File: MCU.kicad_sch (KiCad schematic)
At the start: 14 parts, among them Q15 LMBT3904DW1T1G, SW3 SKRKAEE020, U1 ESP32-S3-WROOM-1U-N16, U15 TPS3831G33DQNR, U3 CH343P

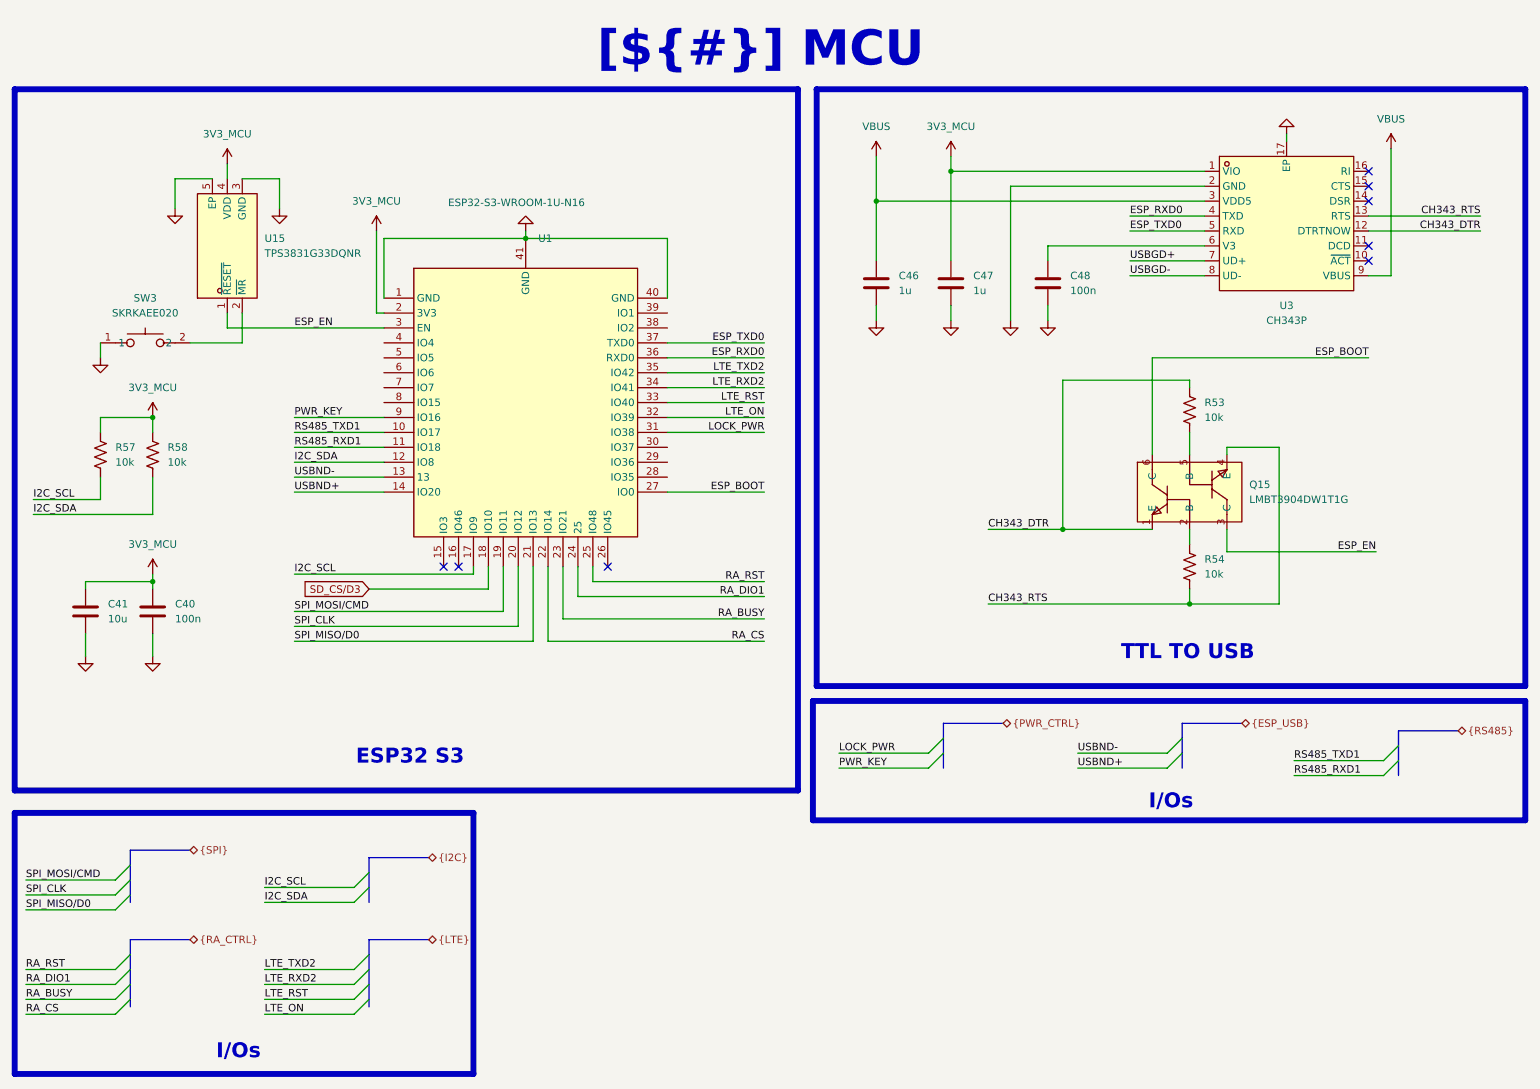
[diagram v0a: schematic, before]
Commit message: [Schematic][Added] Project Architecture, connectors
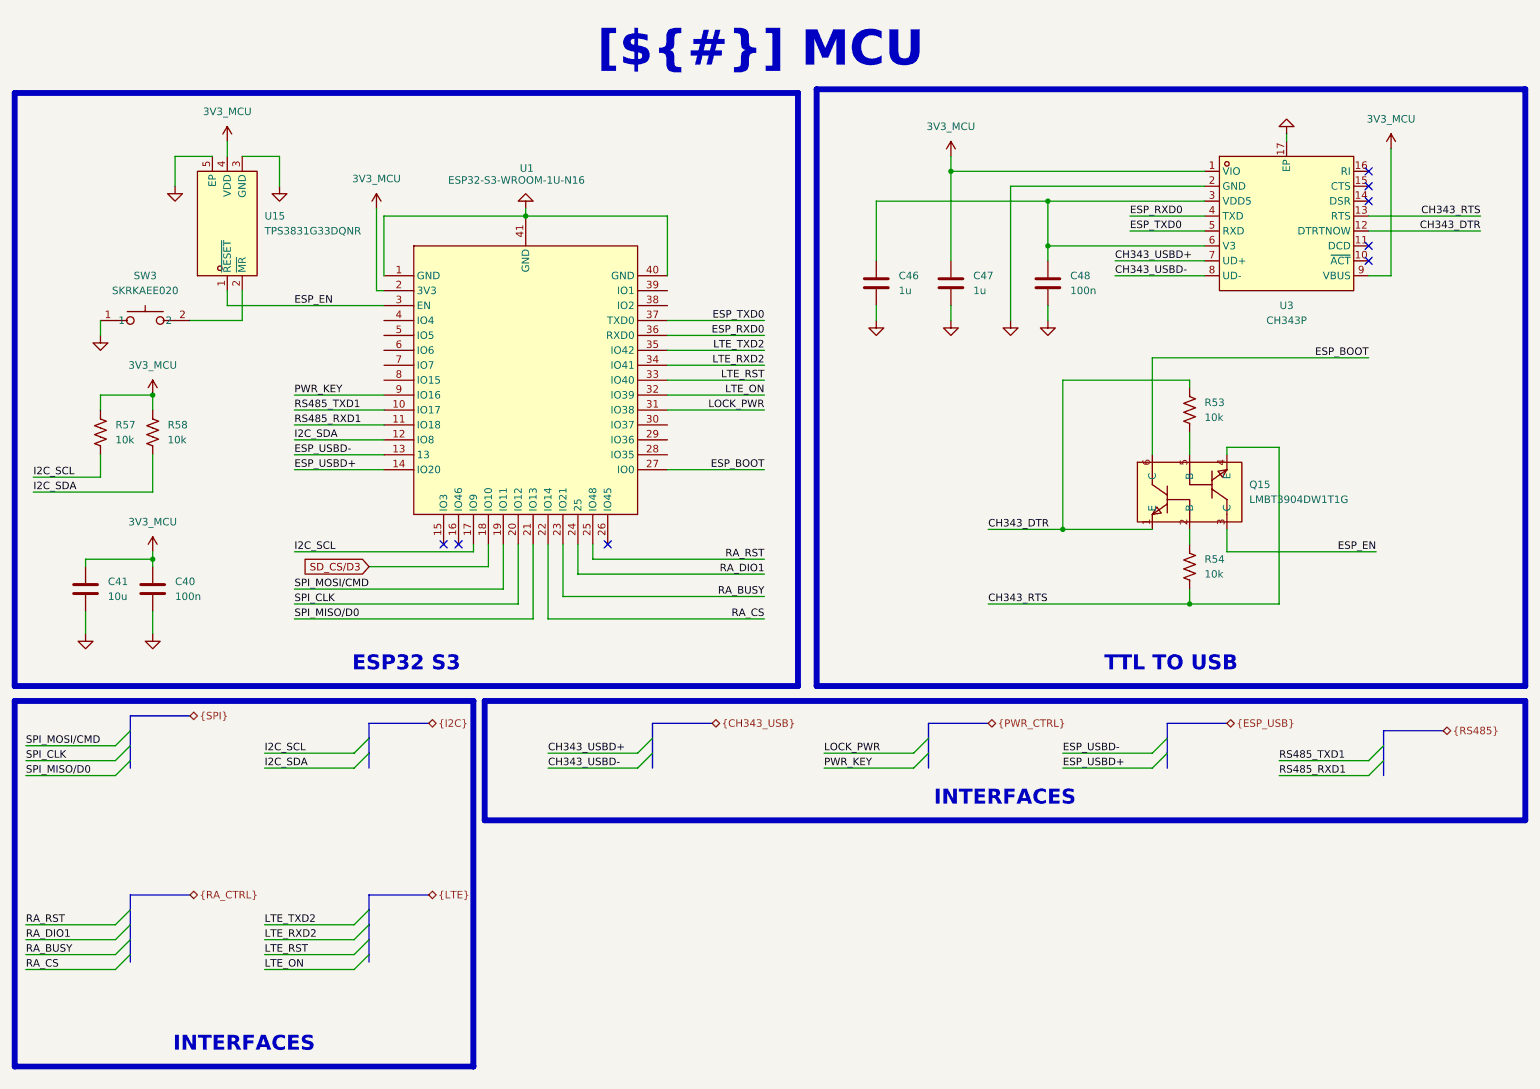
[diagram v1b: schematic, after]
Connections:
- net 3V3_MCU: now also U3.9 (VBUS)
- net at C48.1, U3.6 (V3): now also C46.1, U3.3 (VDD5)
- net USBGD+ renamed CH343_USBD+
- net USBGD- renamed CH343_USBD-
- net USBND+ renamed ESP_USBD+
- net USBND- renamed ESP_USBD-
- removed net VBUS: C46.1, U3.3 (VDD5), U3.9 (VBUS)
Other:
- moved on the sheet: C40, C41, R57, R58, SW3, U1, U15

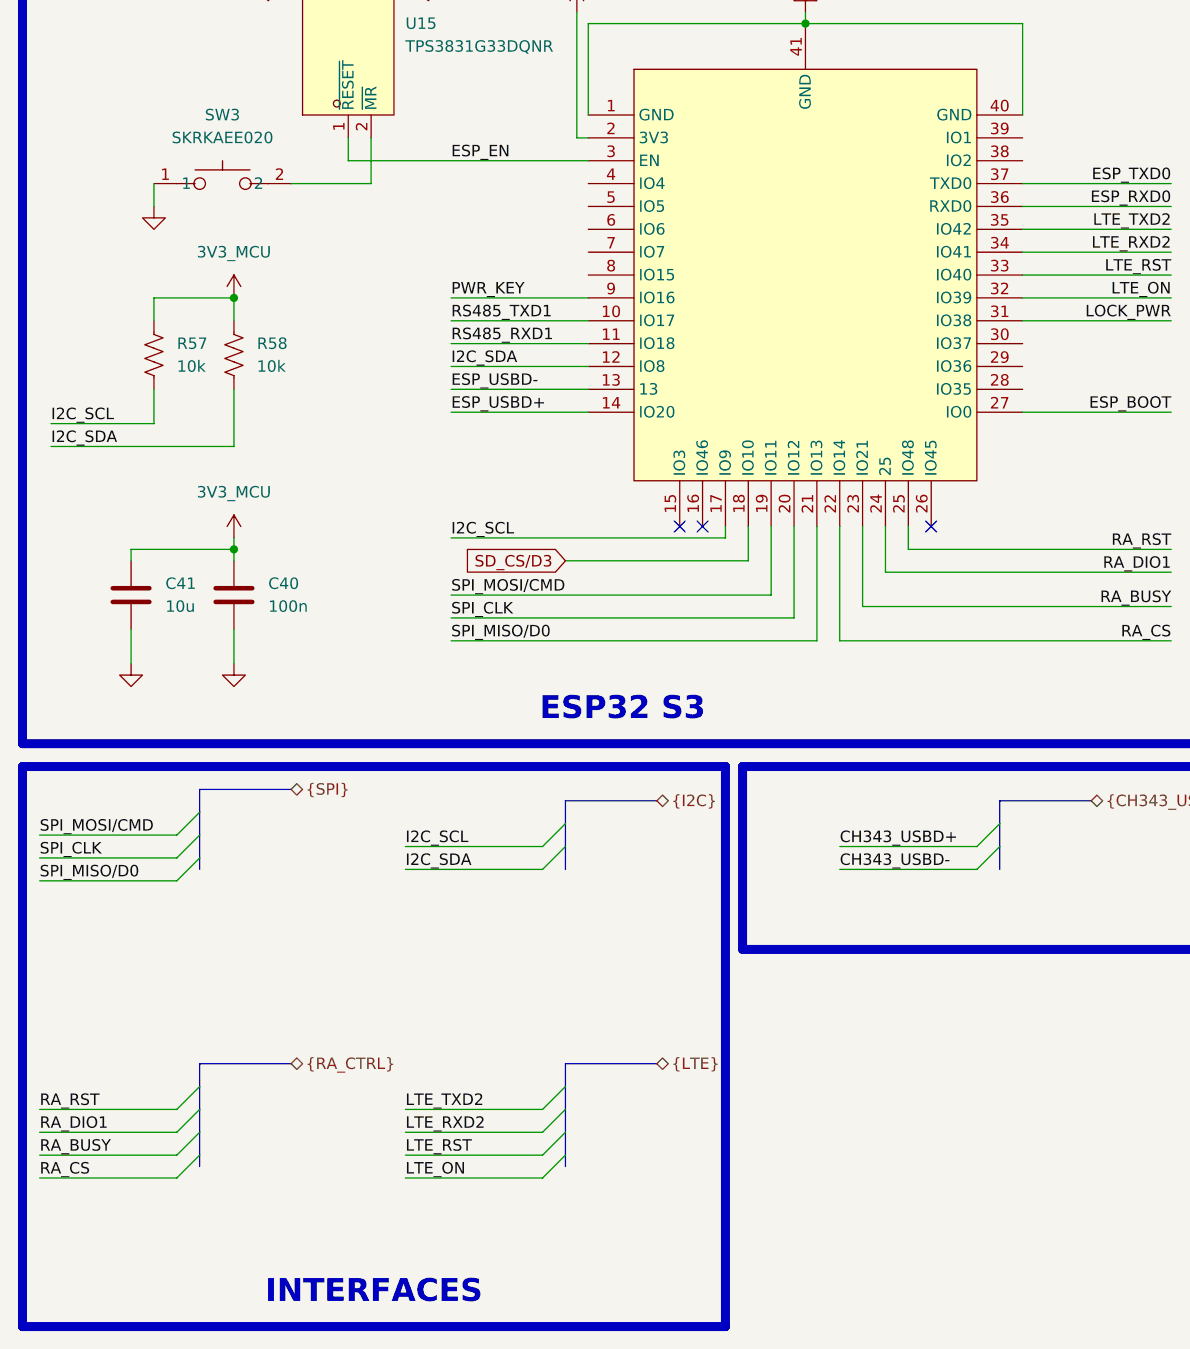
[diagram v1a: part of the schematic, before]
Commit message: [Schematic][Added] Net labels
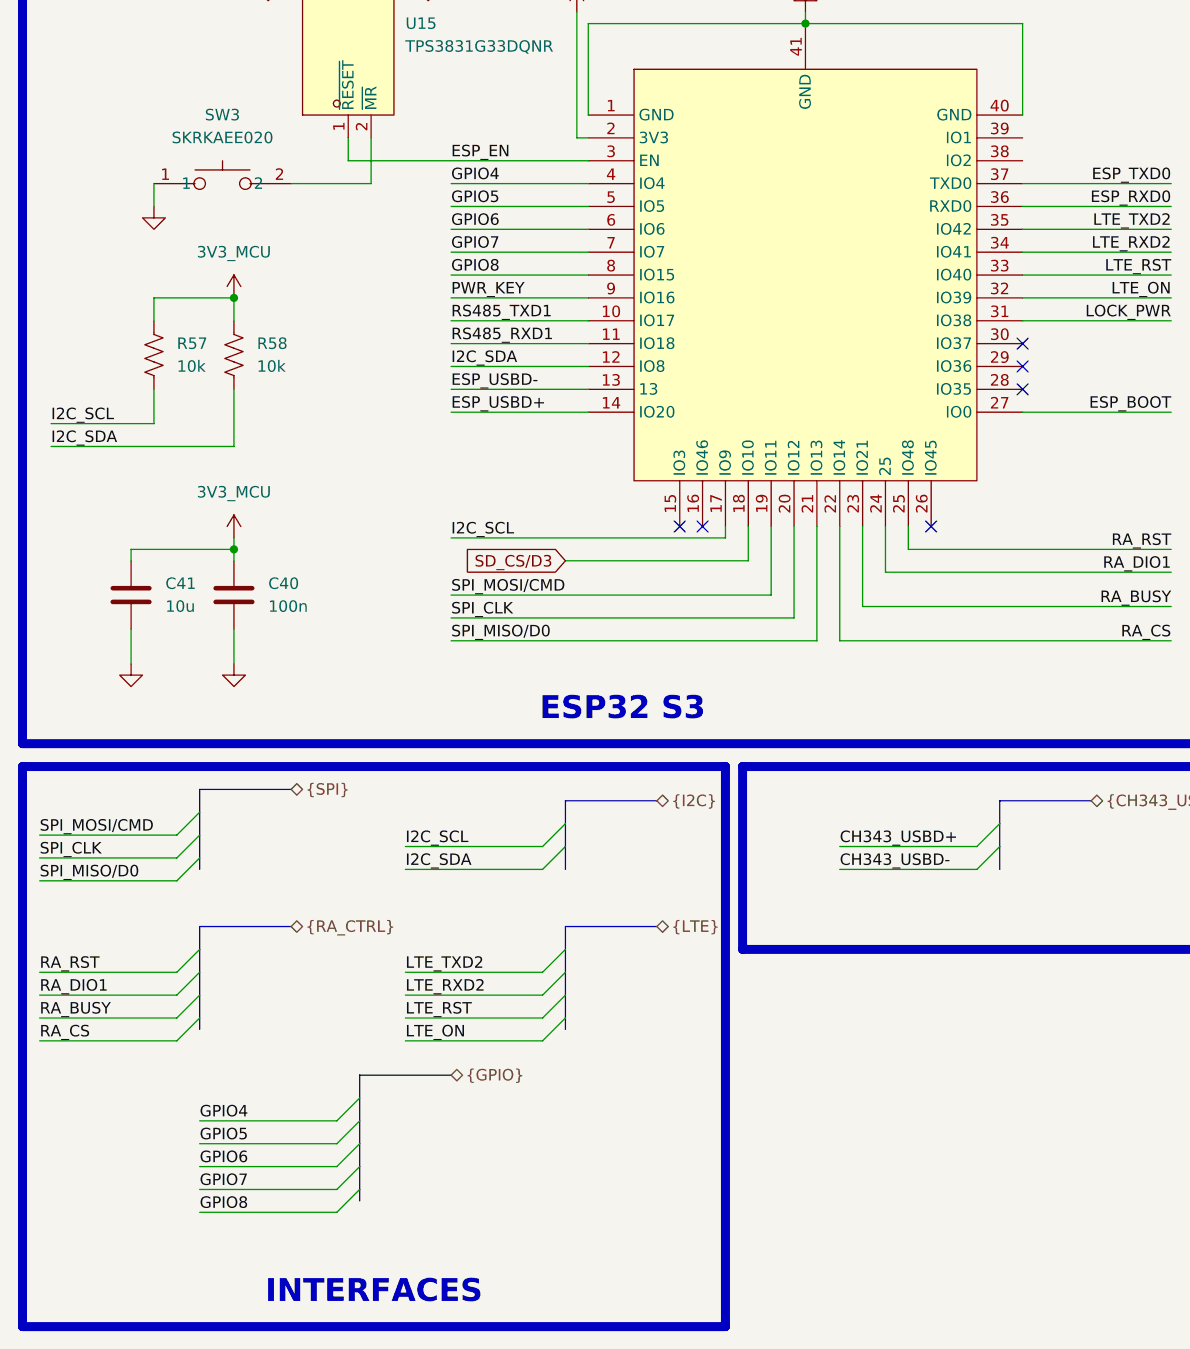
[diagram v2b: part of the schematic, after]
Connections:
- net GPIO4: now reaches U1.4 (IO4)
- net GPIO5: now reaches U1.5 (IO5)
- net GPIO6: now reaches U1.6 (IO6)
- net GPIO7: now reaches U1.7 (IO7)
- net GPIO8: now reaches U1.8 (IO15)
- no-connect marks 8 -> 11

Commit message: [PCB/SCH][Added] Preliminary version
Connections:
- no-connect marks 11 -> 13

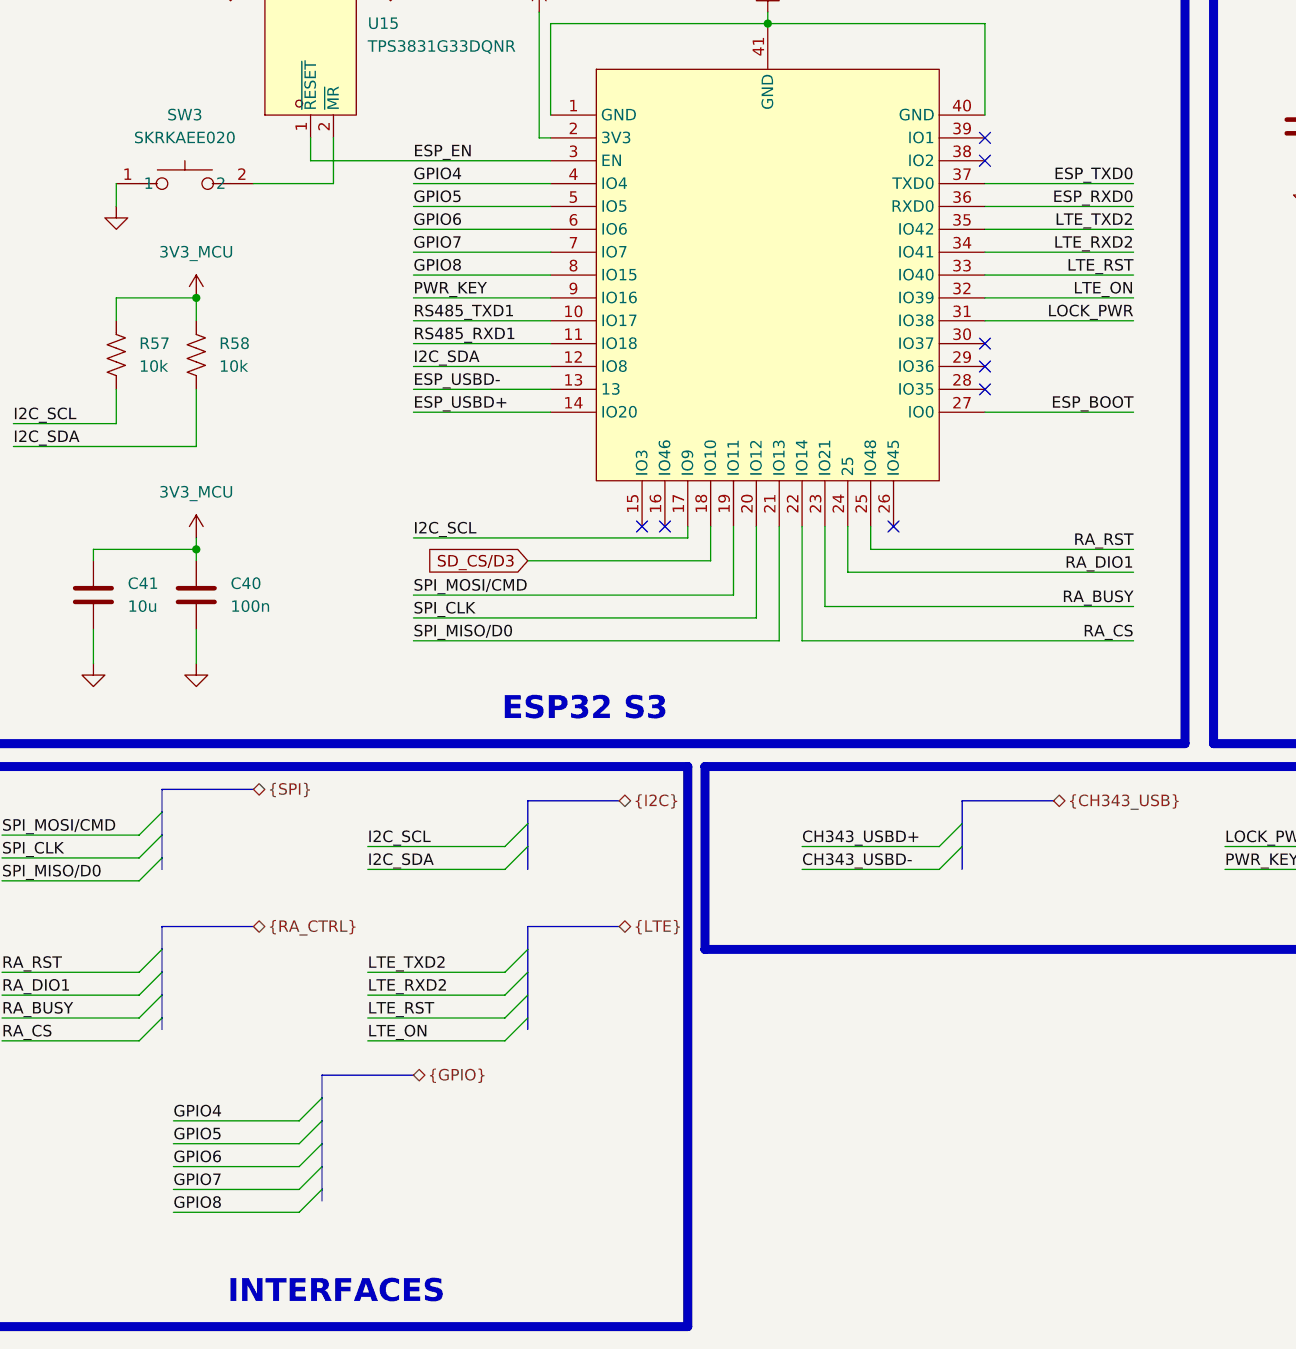
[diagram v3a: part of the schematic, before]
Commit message: [Schematic/PCB][Added] Connectors, layout, preliminar routing
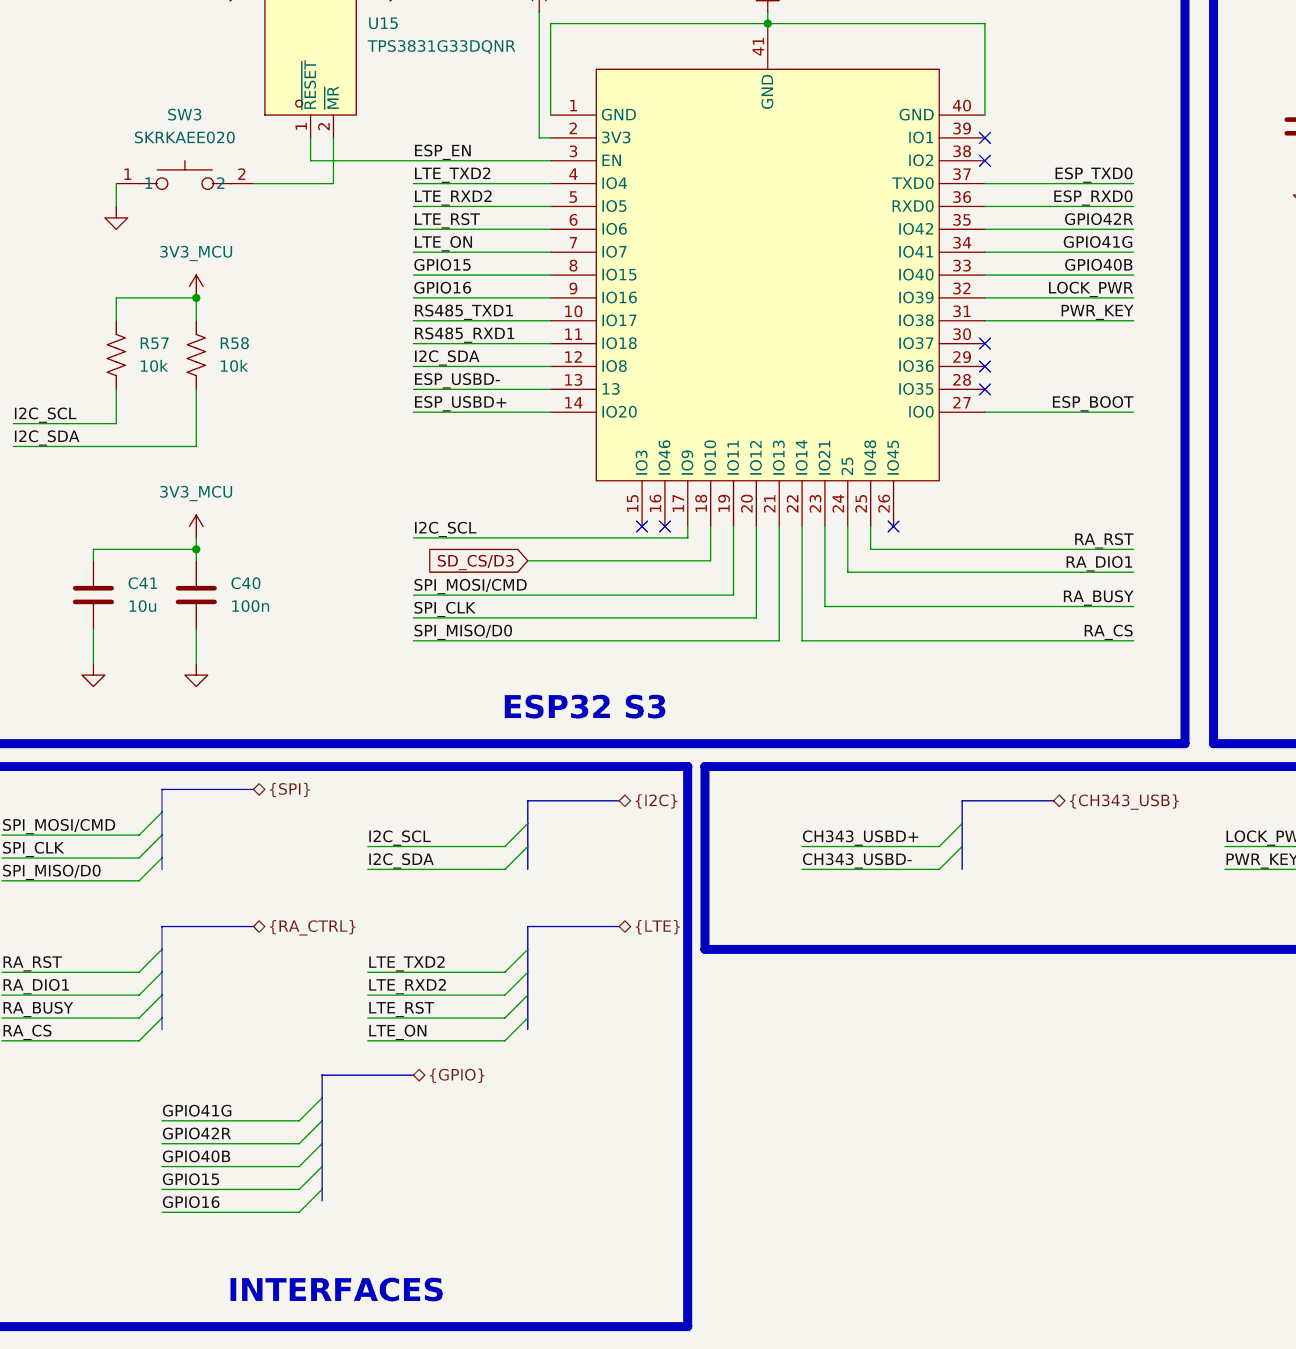
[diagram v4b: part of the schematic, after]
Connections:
- net GPIO4 is gone; now on net LTE_TXD2: U1.4 (IO4)
- net GPIO5 is gone; now on net LTE_RXD2: U1.5 (IO5)
- net GPIO6 is gone; now on net LTE_RST: U1.6 (IO6)
- net GPIO7 is gone; now on net LTE_ON: U1.7 (IO7)
- net LOCK_PWR: now also U1.32 (IO39); no longer U1.31 (IO38)
- net LTE_ON: no longer U1.32 (IO39)
- net LTE_RST: no longer U1.33 (IO40)
- net LTE_RXD2: no longer U1.34 (IO41)
- net LTE_TXD2: no longer U1.35 (IO42)
- net PWR_KEY: now also U1.31 (IO38); no longer U1.9 (IO16)
- net GPIO8 renamed GPIO15
- new net GPIO16: U1.9 (IO16)
- new net GPIO40B: U1.33 (IO40)
- new net GPIO41G: U1.34 (IO41)
- new net GPIO42R: U1.35 (IO42)
